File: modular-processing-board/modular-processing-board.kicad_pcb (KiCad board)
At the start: 6 copper layers, 90 x 90 mm, 166 parts, among them J1001 BWU.FL-IPEX1, J202 Conn_02x06_Odd_Even, J401 TF-01A, J501 Plug_Hirose_DF40_2x40_DF40C-8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, J502 Conn_02x06_Odd_Even, J601 Conn_Coaxial_Small, J602 BWU.FL-IPEX1, J604 Conn_Coaxial_Small, J701 Conn_02x02_Odd_Even, J801 TYPE-C-31-M-12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

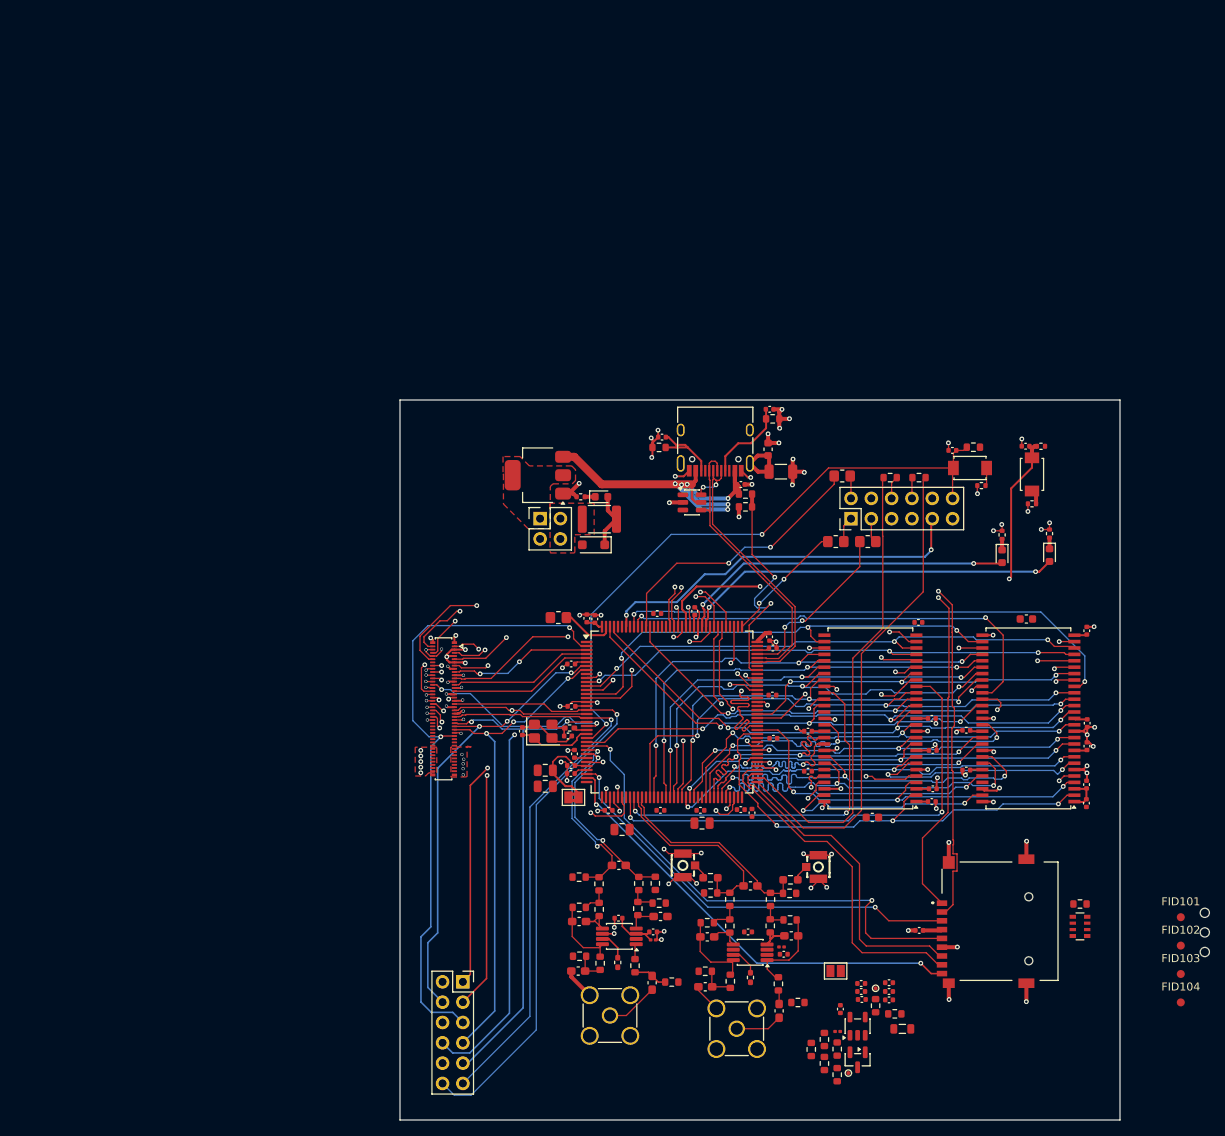
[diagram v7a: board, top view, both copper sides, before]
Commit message: layed out most components (next) cadd vias for impedance reduction for high-speed signals, check impedance of signals
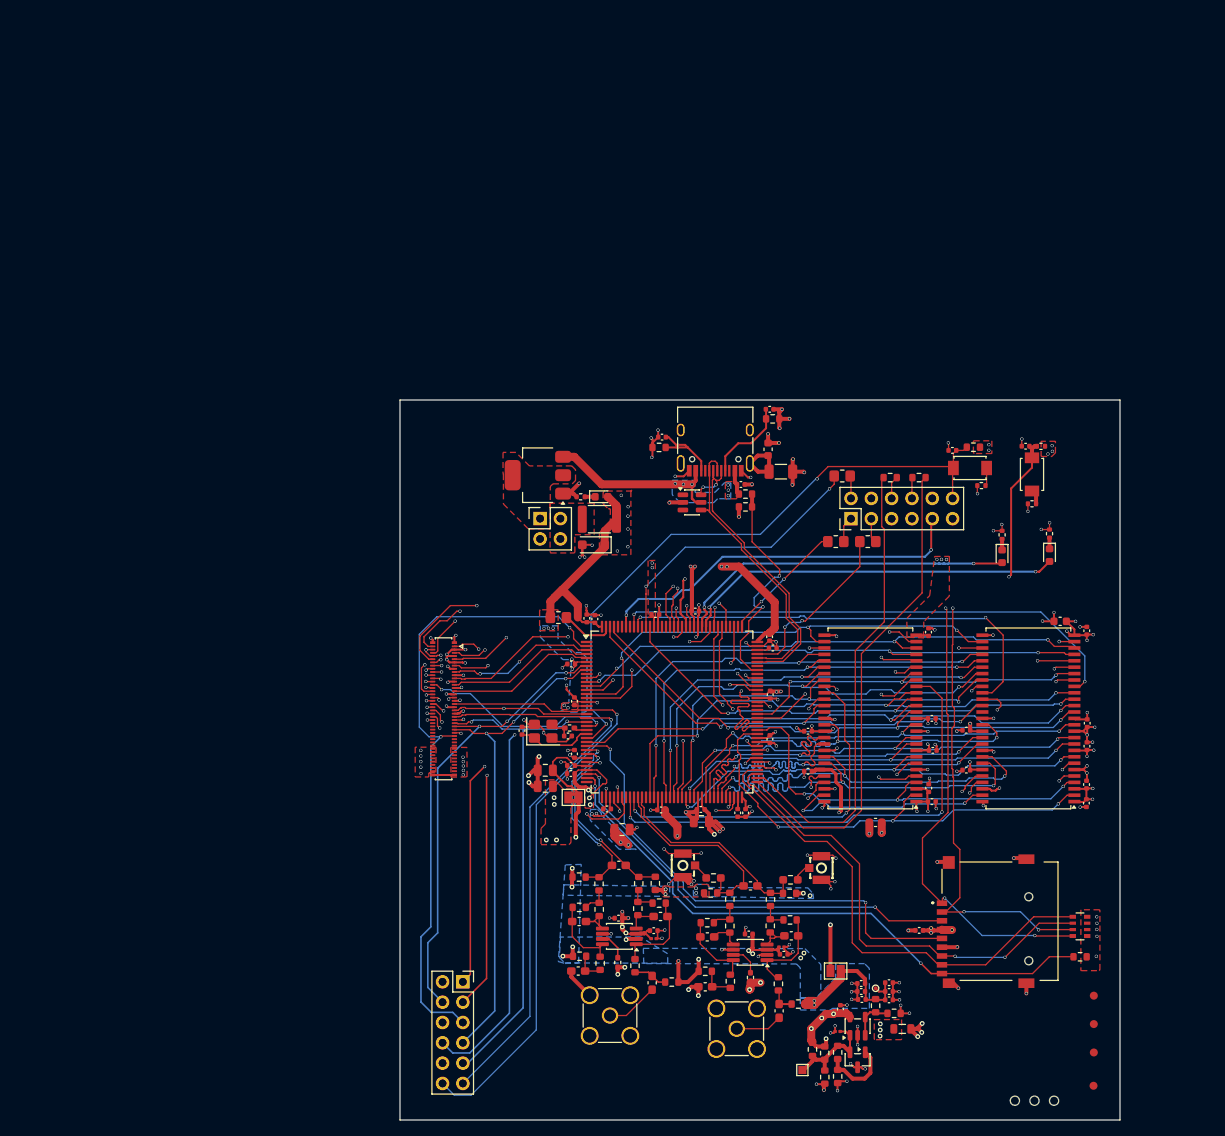
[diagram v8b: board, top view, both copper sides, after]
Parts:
- J401: value TF-01A -> TF01A
- TP601: footprint iw-misc:TestPoint_Pad_D0.5mm -> TestPoint:TestPoint_Pad_1.0x1.0mm
- moved H101 33.4 mm to (124.9, 135.6), turned to 90 degrees
- moved H102 29.9 mm to (127.3, 135.6), turned to 90 degrees
- moved H103 26.5 mm to (129.8, 135.6), turned to 90 degrees
- moved FID104 15.1 mm to (134.7, 133.7)
- moved FID102 14.6 mm to (134.7, 126.0)
- moved FID103 14.6 mm to (134.7, 129.6)
- moved FID101 14.6 mm to (134.7, 122.5)
- moved R401 6.60 mm to (133.0, 117.6)
- moved TP601 5.77 mm to (98.3, 131.8), turned to 0 degrees
- moved R607 4.91 mm to (102.7, 132.6), turned to -90 degrees
- moved C312 4.23 mm to (130.5, 75.7), turned to 180 degrees
- moved R604 2.16 mm to (102.7, 129.6), turned to -90 degrees
- moved C1101 1.75 mm to (114.1, 77.0), turned to 90 degrees
- moved R603 1.64 mm to (101.1, 129.6)
- moved R606 1.58 mm to (101.1, 132.6)
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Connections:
- net /adc-frontend/ADC_VOCM_REF renamed /adc-frontend/VOCM_REF
- C603 pad 2: /adc-frontend/ADC_VOCM_BUFF -> /adc-frontend/VOCM_BUFF
- C604 pad 1: /adc-frontend/ADC_VOCM_BUFF -> /adc-frontend/VOCM_BUFF
- C605 pad 1: /adc-frontend/ADC_VOCM_BUFF -> /adc-frontend/VOCM_BUFF
- C606 pad 1: /adc-frontend/ADC_VOCM_BUFF -> /adc-frontend/VOCM_BUFF
- C607 pad 1: /adc-frontend/ADC_VOCM_BUFF -> /adc-frontend/VOCM_BUFF
- C608 pad 1: /adc-frontend/ADC_VOCM_BUFF -> /adc-frontend/VOCM_BUFF
- JP602 pad 1: /adc-frontend/ADC_VOCM_BUFF -> /adc-frontend/VOCM_BUFF
- R602 pad 1: /adc-frontend/ADC_VOCM_BUFF -> /adc-frontend/VOCM_BUFF
- TP602 pad 1: /adc-frontend/ADC_VOCM_BUFF -> /adc-frontend/VOCM_BUFF
- U201 pad 9: /mcu/USB_SENSE -> unconnected-(U201-PC15-Pad9)
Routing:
- net +3V3: track 41.6 -> 158.1 mm, vias 0 -> 70
- net GND: track 174.3 -> 243.9 mm, vias 111 -> 162
- net /adc-frontend/MCU_VREF: track 11.2 -> 60.3 mm, vias 0 -> 2
- net /adc-frontend/VOCM_BUFF: track 0.00 -> 38.7 mm, vias 0 -> 18
- net VDDA: track 8.68 -> 41.3 mm, vias 0 -> 24
- net /usb/USB_SH: track 7.58 -> 33.9 mm
- net /power/USB_VBUS: track 50.8 -> 26.5 mm
- net /mcu/SDRAM.D14: track 28.4 -> 52.0 mm, vias 2 -> 3
- net /mcu/SDMMC.D1: track 43.0 -> 61.8 mm
- net /mcu/SDMMC.CD: track 56.2 -> 74.5 mm
- net /mcu/SDMMC.D0: track 40.7 -> 58.9 mm, vias 0 -> 2
- net /mcu/SDMMC.D2: track 80.7 -> 98.3 mm, vias 2 -> 4
- net /mcu/SDMMC.D3: track 82.1 -> 99.5 mm, vias 2 -> 4
- net /adc-frontend/VOCM_REF: track 0.00 -> 13.4 mm
- net /mcu/SDRAM.CLK: track 48.4 -> 37.7 mm
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- added copper zone on B.Cu, net +3V3
- added copper zone on F.Cu, net +3V3
- added copper zone on In3.Cu, net +3V3
- added copper zone on B.Cu, net /adc-frontend/VOCM_BUFF
- added copper zone on F.Cu, net /adc-frontend/VOCM_BUFF
- added copper zone on In3.Cu, net /adc-frontend/VOCM_BUFF
- added copper zone on B.Cu, net /power/USB_VBUS
- added copper zone on F.Cu, net /power/USB_VBUS
- added copper zone on F.Cu, net VDDA
- added copper zone on In3.Cu, net VDDA
